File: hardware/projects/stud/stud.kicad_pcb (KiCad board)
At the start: 2 copper layers, 3 parts, among them IC1 R7KA8M2JFLCAC#UC0, U1 IS42VM32160E-75BLI, U2 TAC5242

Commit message: switch to four layers
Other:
- copper layers 2 -> 4
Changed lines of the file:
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@@
 	(layers
 		(0 "F.Cu" signal)
+		(4 "In1.Cu" signal)
+		(6 "In2.Cu" signal)
 		(2 "B.Cu" signal)
 		(9 "F.Adhes" user "F.Adhesive")
@@
 			)
 			(layer "dielectric 1"
-				(type "core")
-				(thickness 1.51)
+				(type "prepreg")
+				(thickness 0.1)
 				(material "FR4")
 				(epsilon_r 4.5)
+				(loss_tangent 0.02)
+			)
+			(layer "In1.Cu"
+				(type "copper")
+				(thickness 0.035)
+			)
+			(layer "dielectric 2"
+				(type "core")
+				(thickness 1.24)
+				(material "FR4")
+				(epsilon_r 4.5)
+				(loss_tangent 0.02)
+			)
+			(layer "In2.Cu"
+				(type "copper")
+				(thickness 0.035)
+			)
+			(layer "dielectric 3"
+				(type "prepreg")
+				(thickness 0.1)
+				(material "FR4")
+				(epsilon_r 4.5)

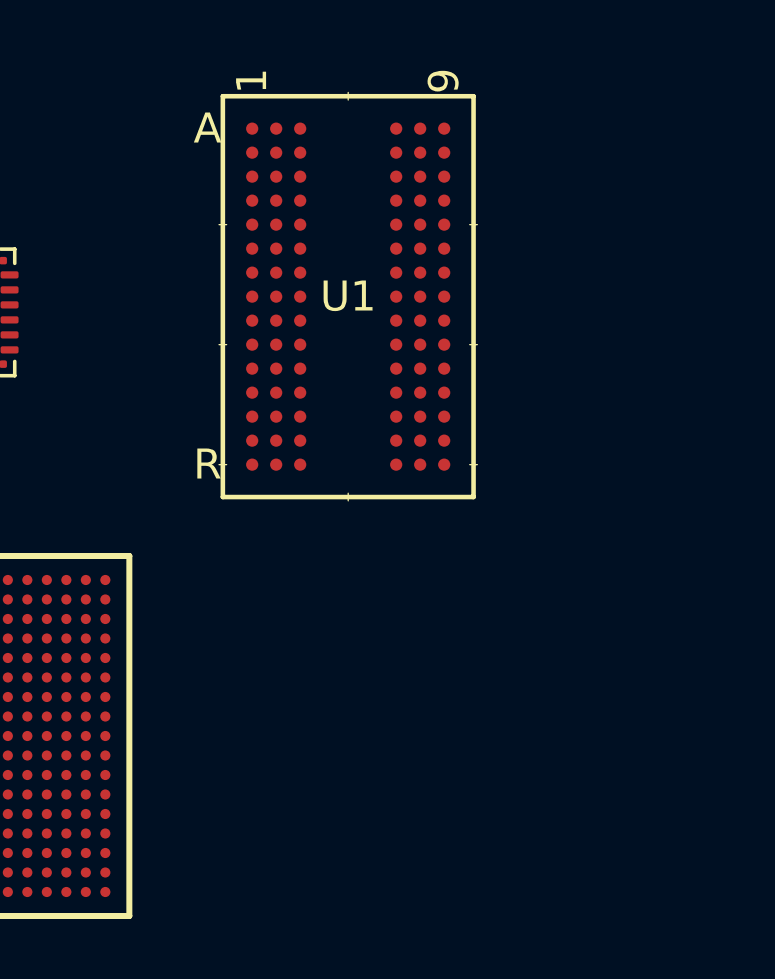
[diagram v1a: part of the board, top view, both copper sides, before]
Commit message: switch SDRAM chips at fable's behest
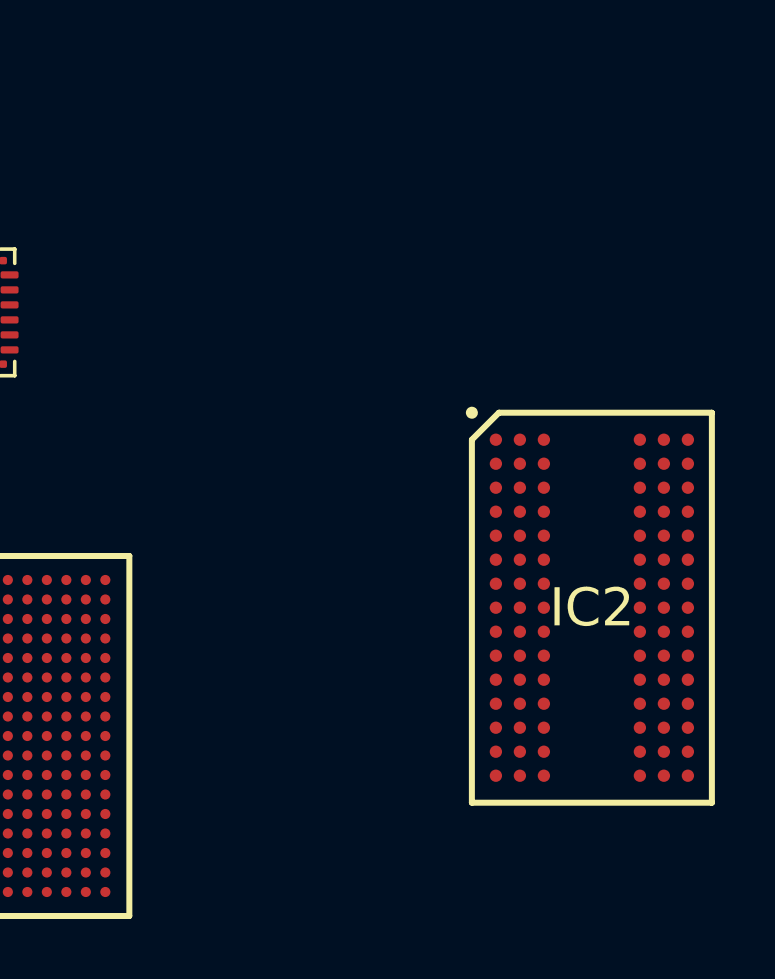
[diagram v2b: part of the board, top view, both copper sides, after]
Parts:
- removed U1: IS42VM32160E-75BLI, vendor:TFBGA-90_8X13_ISI
- added IC2: IS42S32160F-7BLI, vendor:BGA90C80P9X15_800X1300X120, F.Cu at (155.4, 106.9)

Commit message: think about routing SDRAM traces
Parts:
- moved IC2 8.45 mm to (147.3, 109.2)
- moved IC1 2.03 mm to (134.6, 109.2)
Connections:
- IC1 pad L3: unconnected-(IC1-PC04-PadL3) -> DQ26
- IC1 pad L4: unconnected-(IC1-PC09-PadL4) -> DQ21
- IC1 pad L5: unconnected-(IC1-PC05-PadL5) -> DQ25
- IC2 pad A1: unconnected-(IC2-DQ26-PadA1) -> DQ26
- IC2 pad A9: unconnected-(IC2-DQ21-PadA9) -> DQ21
- IC2 pad C3: unconnected-(IC2-DQ25-PadC3) -> DQ25
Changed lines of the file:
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@@
 	(layers
 		(0 "F.Cu" signal)
-		(4 "In1.Cu" signal)
-		(6 "In2.Cu" signal)
+		(4 "In1.Cu" power)
+		(6 "In2.Cu" power)
 		(2 "B.Cu" signal)
 		(9 "F.Adhes" user "F.Adhesive")
@@
 	(footprint "vendor:BGA90C80P9X15_800X1300X120"
 		(layer "F.Cu")
-		(at 155.443 106.889)
+		(at 147.32 109.22)
 		(descr "90L 8x13mm TF-BGA")
 		(tags "Integrated Circuit")
@@
 		(sheetname "/")
 		(sheetfile "stud.kicad_sch")
+		(units
+			(unit
+				(name "A")
+				(pins "A1" "A2" "A3" "A7" "A8" "A9" "B1" "B2" "B3" "B7" "B8" "B9" "C1"
+					"C2" "C3" "C7" "C8" "C9" "D1" "D2" "D3" "D7" "D8" "D9" "E1" "E2" "E3"
+					"E7" "E8" "E9" "F1" "F2" "F3" "F7" "F8" "F9" "G1" "G2" "G3" "G7" "G8"
+					"G9" "H1" "H2" "H3" "H7" "H8" "H9" "J1" "J2" "J3" "J7" "J8" "J9" "K1"
+					"K2" "K3" "K7" "K8" "K9" "L1" "L2" "L3" "L7" "L8" "L9" "M1" "M2" "M3"
+					"M7" "M8" "M9" "N1" "N2" "N3" "N7" "N8" "N9" "P1" "P2" "P3" "P7" "P8"
+					"P9" "R1" "R2" "R3" "R7" "R8" "R9"
+				)
+			)
+		)
 		(solder_mask_margin 0.035)
 		(attr smd)
@@
 			(size 0.41 0.41)
 			(layers "F.Cu" "F.Mask" "F.Paste")
-			(net "unconnected-(IC2-DQ26-PadA1)")
+			(net "DQ26")
 			(pinfunction "DQ26_A1")
 			(pintype "passive")
@@
 			(size 0.41 0.41)
 			(layers "F.Cu" "F.Mask" "F.Paste")
-			(net "unconnected-(IC2-DQ21-PadA9)")
+			(net "DQ21")
 			(pinfunction "DQ21_A9")
 			(pintype "passive")
@@
 			(size 0.41 0.41)
 			(layers "F.Cu" "F.Mask" "F.Paste")
-			(net "unconnected-(IC2-DQ25-PadC3)")
+			(net "DQ25")
 			(pinfunction "DQ25_C3")
 			(pintype "passive")
@@
 	(footprint "vendor:BGA289C65P17X17_1200X1200X138"
 		(layer "F.Cu")
-		(at 134.025 111.165)
+		(at 134.62 109.22)
 		(descr "PLBG0289JA-A")
 		(tags "Integrated Circuit")
@@
 			(size 0.338 0.338)
 			(layers "F.Cu" "F.Mask" "F.Paste")
-			(net "unconnected-(IC1-PC04-PadL3)")
+			(net "DQ26")
 			(pinfunction "PC04_L3")
 			(pintype "passive")
@@
 			(size 0.338 0.338)
 			(layers "F.Cu" "F.Mask" "F.Paste")
-			(net "unconnected-(IC1-PC09-PadL4)")
+			(net "DQ21")
 			(pinfunction "PC09_L4")
 			(pintype "passive")
@@
 			(size 0.338 0.338)
 			(layers "F.Cu" "F.Mask" "F.Paste")
-			(net "unconnected-(IC1-PC05-PadL5)")
+			(net "DQ25")
 			(pinfunction "PC05_L5")
 			(pintype "passive")

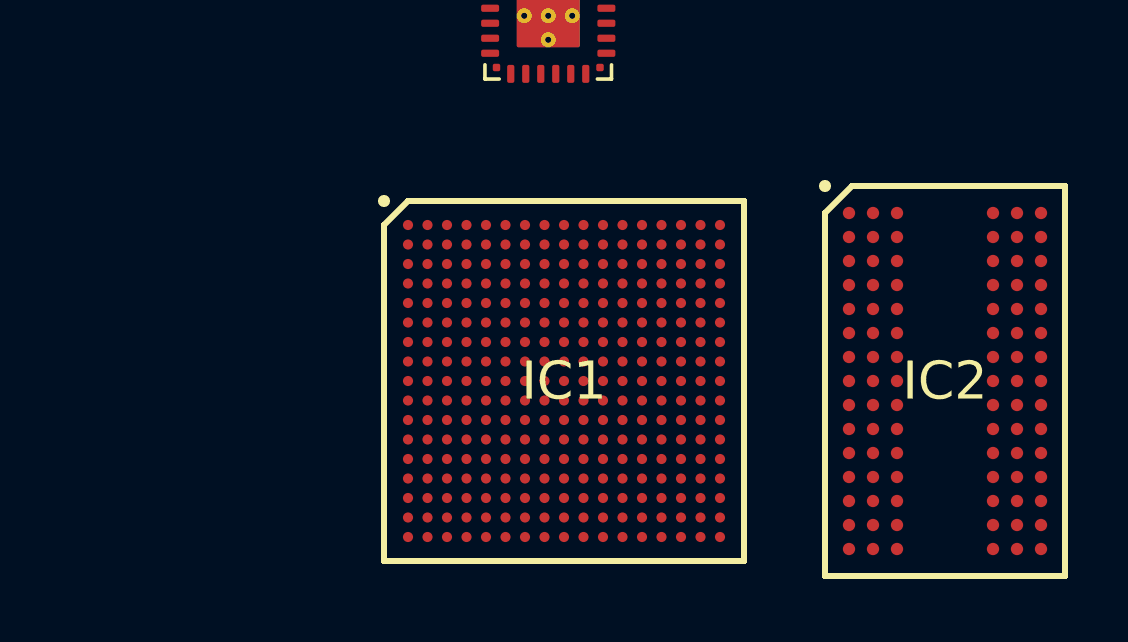
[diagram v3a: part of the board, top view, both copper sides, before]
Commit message: add enough DQ nets to peek at connections
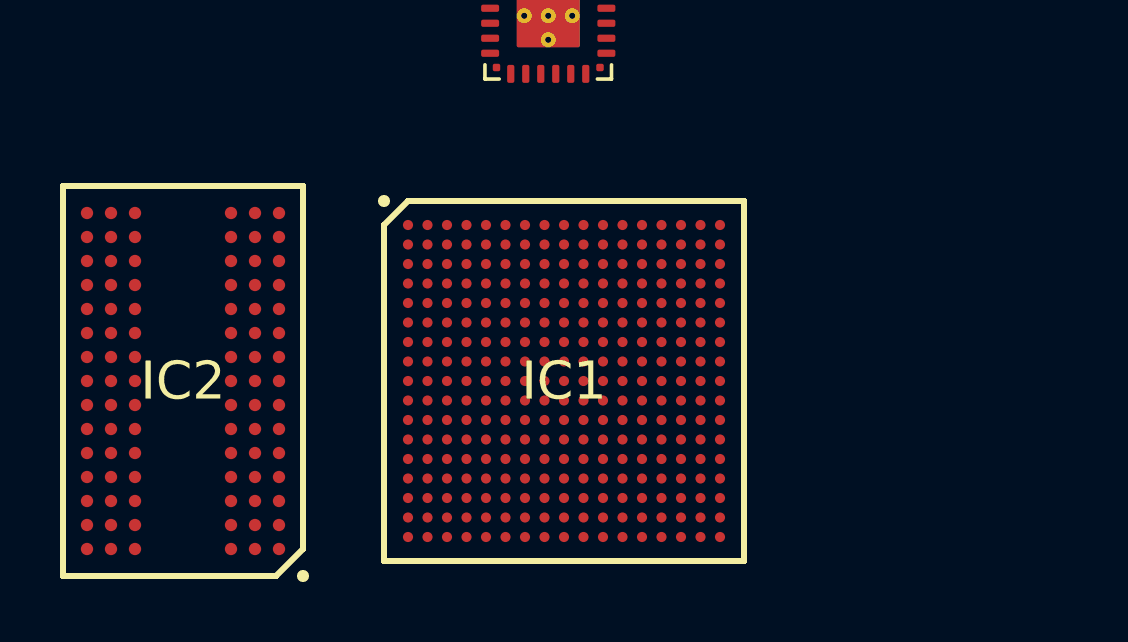
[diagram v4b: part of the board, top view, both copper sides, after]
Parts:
- moved IC2 25.4 mm to (121.9, 109.2), turned to 180 degrees
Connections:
- IC1 pad A1: unconnected-(IC1-P609-PadA1) -> DQ7
- IC1 pad A2: unconnected-(IC1-P113-PadA2) -> DQ4
- IC1 pad A3: unconnected-(IC1-P115-PadA3) -> DQ6
- IC1 pad A4: unconnected-(IC1-P112-PadA4) -> DQ3
- IC1 pad A5: unconnected-(IC1-P302-PadA5) -> DQ0
- IC1 pad B2: unconnected-(IC1-PA12-PadB2) -> DQ9
- IC1 pad B3: unconnected-(IC1-P114-PadB3) -> DQ5
- IC1 pad B4: unconnected-(IC1-PA11-PadB4) -> DQ8
- IC1 pad B5: unconnected-(IC1-P300-PadB5) -> DQ2
- IC1 pad C3: unconnected-(IC1-PA13-PadC3) -> DQ15
- IC2 pad A2: unconnected-(IC2-DQ24-PadA2) -> DQ24
- IC2 pad A8: unconnected-(IC2-DQ23-PadA8) -> DQ23
- IC2 pad B1: unconnected-(IC2-DQ28-PadB1) -> DQ28
- IC2 pad B9: unconnected-(IC2-DQ19-PadB9) -> DQ19
- IC2 pad C2: unconnected-(IC2-DQ27-PadC2) -> DQ27
- IC2 pad C7: unconnected-(IC2-DQ22-PadC7) -> DQ22
- IC2 pad C8: unconnected-(IC2-DQ20-PadC8) -> DQ20
- IC2 pad D2: unconnected-(IC2-DQ29-PadD2) -> DQ29
- IC2 pad D3: unconnected-(IC2-DQ30-PadD3) -> DQ30
- IC2 pad D7: unconnected-(IC2-DQ17-PadD7) -> DQ17
- IC2 pad D8: unconnected-(IC2-DQ18-PadD8) -> DQ18
- IC2 pad E2: unconnected-(IC2-DQ31-PadE2) -> DQ31
- IC2 pad E8: unconnected-(IC2-DQ16-PadE8) -> DQ16
- IC2 pad L2: unconnected-(IC2-DQ8-PadL2) -> DQ8
- IC2 pad L8: unconnected-(IC2-DQ7-PadL8) -> DQ7
- IC2 pad M2: unconnected-(IC2-DQ10-PadM2) -> DQ10
- IC2 pad M3: unconnected-(IC2-DQ9-PadM3) -> DQ9
- IC2 pad M7: unconnected-(IC2-DQ6-PadM7) -> DQ6
- IC2 pad M8: unconnected-(IC2-DQ5-PadM8) -> DQ5
- IC2 pad N2: unconnected-(IC2-DQ12-PadN2) -> DQ12
- IC2 pad N3: unconnected-(IC2-DQ14-PadN3) -> DQ14
- IC2 pad N7: unconnected-(IC2-DQ1-PadN7) -> DQ1
- IC2 pad N8: unconnected-(IC2-DQ3-PadN8) -> DQ3
- IC2 pad P1: unconnected-(IC2-DQ11-PadP1) -> DQ11
- IC2 pad P9: unconnected-(IC2-DQ4-PadP9) -> DQ4
- IC2 pad R1: unconnected-(IC2-DQ13-PadR1) -> DQ13
- IC2 pad R2: unconnected-(IC2-DQ15-PadR2) -> DQ15
- IC2 pad R8: unconnected-(IC2-DQ0-PadR8) -> DQ0
- IC2 pad R9: unconnected-(IC2-DQ2-PadR9) -> DQ2

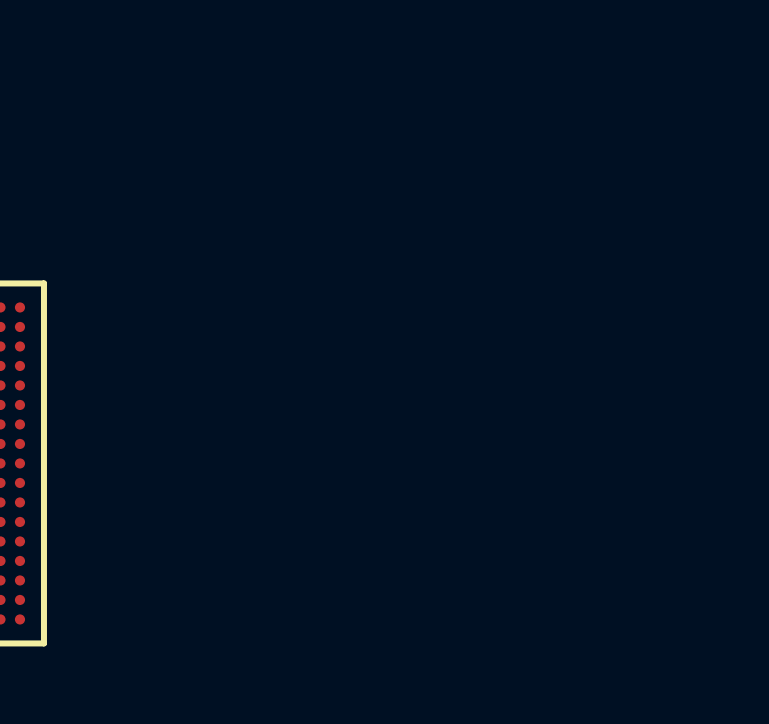
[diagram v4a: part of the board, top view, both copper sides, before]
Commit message: add a microSD connector
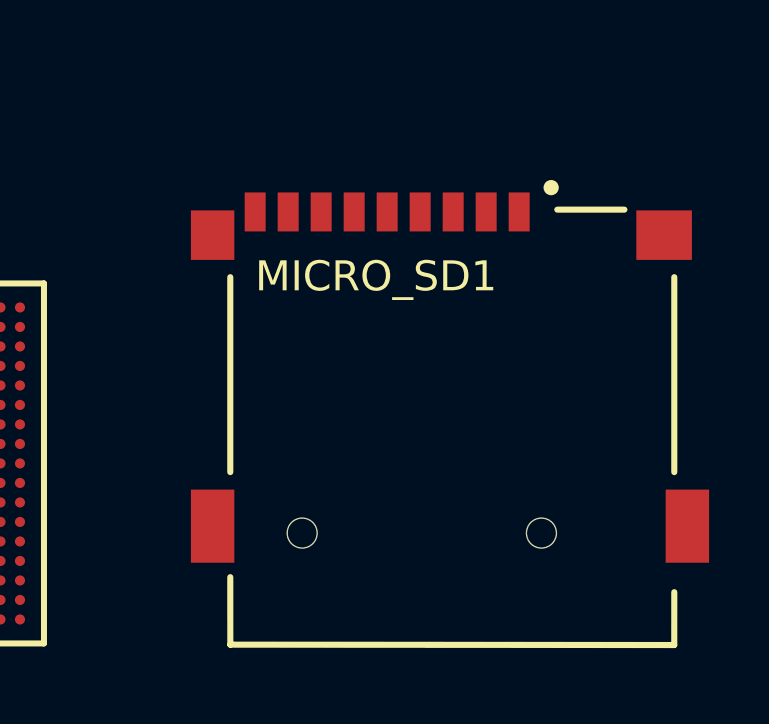
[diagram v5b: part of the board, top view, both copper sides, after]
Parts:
- added MICRO_SD1: TF-01A, vendor:TF-01A, F.Cu at (154.2, 108.0)

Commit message: add a buck converter
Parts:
- added U1: TPS629210DRLR, vendor:SOT50P160X60-8N, F.Cu at (141.5, 95.3)

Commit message: add a castellated edge gpio footprint
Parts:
- added J1: USB_C_Receptacle_USB2.0_16P, Connector_USB:USB_C_Receptacle_G-Switch_GT-USB-7010ASV, F.Cu at (180.6, 106.5)
- added Y1: X1G0044510004, custom:SG5032CAN, F.Cu at (178.3, 113.7)
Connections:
- IC1 pad A10: unconnected-(IC1-VCC_D_CDC_1-PadA10) -> +3V3
- IC1 pad A11: unconnected-(IC1-VCC_D_CDC_2-PadA11) -> +3V3
- IC1 pad A7: unconnected-(IC1-VLO_1-PadA7) -> VLO
- IC1 pad A8: unconnected-(IC1-VLO_2-PadA8) -> VLO
- IC1 pad A9: unconnected-(IC1-VSS_D_CDC_1-PadA9) -> GND
- IC1 pad B1: unconnected-(IC1-P813-PadB1) -> SDCS
- IC1 pad B10: unconnected-(IC1-VCC_D_CDC_3-PadB10) -> +3V3
- IC1 pad B11: unconnected-(IC1-VCC_D_CDC_4-PadB11) -> +3V3
- IC1 pad B16: unconnected-(IC1-PD01-PadB16) -> μSD_DAT2
- IC1 pad B17: unconnected-(IC1-PD02-PadB17) -> μSD_DAT1
- IC1 pad B7: unconnected-(IC1-VLO_3-PadB7) -> VLO
- IC1 pad B8: unconnected-(IC1-VLO_4-PadB8) -> VLO
- IC1 pad B9: unconnected-(IC1-VSS_D_CDC_2-PadB9) -> GND
- IC1 pad C1: unconnected-(IC1-PA06-PadC1) -> CKE
- IC1 pad C14: unconnected-(IC1-PD04-PadC14) -> μSD_CMD
- IC1 pad C15: unconnected-(IC1-PD03-PadC15) -> μSD_DAT0
- IC1 pad C16: unconnected-(IC1-PD05-PadC16) -> μSD_CLK
- IC1 pad C2: unconnected-(IC1-P613-PadC2) -> DQ15
- IC1 pad C3: DQ15 -> DQ10
- IC1 pad C4: unconnected-(IC1-P301-PadC4) -> DQ1
- IC1 pad D1: unconnected-(IC1-PA04-PadD1) -> DQM3
- IC1 pad D11: unconnected-(IC1-P306-PadD11) -> μSD_CD
- IC1 pad D2: unconnected-(IC1-P611-PadD2) -> DQ13
- IC1 pad D3: unconnected-(IC1-P610-PadD3) -> DQ12
- IC1 pad D4: unconnected-(IC1-PA14-PadD4) -> DQ11
- IC1 pad E1: unconnected-(IC1-PA15-PadE1) -> SDCLK
- IC1 pad E2: unconnected-(IC1-P615-PadE2) -> DQM2
- IC1 pad E3: unconnected-(IC1-P614-PadE3) -> DQM0
- IC1 pad E4: unconnected-(IC1-P612-PadE4) -> DQ14
- IC1 pad E8: unconnected-(IC1-P111-PadE8) -> μSD_DAT3
- IC1 pad F1: unconnected-(IC1-PA02-PadF1) -> A3
- IC1 pad F10: unconnected-(IC1-VSS_07-PadF10) -> GND
- IC1 pad F11: unconnected-(IC1-VCC_07-PadF11) -> +3V3
- IC1 pad F14: unconnected-(IC1-P406-PadF14) -> SSI_RX
- IC1 pad F2: unconnected-(IC1-PA10-PadF2) -> RAS
- IC1 pad F3: unconnected-(IC1-PA08-PadF3) -> WE
- IC1 pad F4: unconnected-(IC1-PA09-PadF4) -> CAS
- IC1 pad F5: unconnected-(IC1-PC14-PadF5) -> DQ16
- IC1 pad F6: unconnected-(IC1-VCC_08-PadF6) -> +3V3
- IC1 pad F7: unconnected-(IC1-VSS_08-PadF7) -> GND
- IC1 pad F8: unconnected-(IC1-VSS3-PadF8) -> GND
- IC1 pad G1: unconnected-(IC1-PA00-PadG1) -> A5
- IC1 pad G10: unconnected-(IC1-VSS_06-PadG10) -> GND
- IC1 pad G11: unconnected-(IC1-VCC_06-PadG11) -> +3V3
- IC1 pad G12: unconnected-(IC1-P405-PadG12) -> SSI_TX
- IC1 pad G15: unconnected-(IC1-VSS_03-PadG15) -> GND
- IC1 pad G16: unconnected-(IC1-VCC_05-PadG16) -> +3V3
- IC1 pad G17: unconnected-(IC1-VSS_05-PadG17) -> GND
- IC1 pad G2: unconnected-(IC1-PA03-PadG2) -> A2
- IC1 pad G3: unconnected-(IC1-PA05-PadG3) -> DQM1
- IC1 pad G5: unconnected-(IC1-PC12-PadG5) -> DQ18
- IC1 pad G6: unconnected-(IC1-VCC_09-PadG6) -> +3V3
- IC1 pad G7: unconnected-(IC1-VSS_09-PadG7) -> GND
- IC1 pad G8: unconnected-(IC1-VSS4-PadG8) -> GND
- IC1 pad G9: unconnected-(IC1-VCL4-PadG9) -> +0V9
- IC1 pad H1: unconnected-(IC1-P504-PadH1) -> A7
- IC1 pad H10: unconnected-(IC1-VSS5-PadH10) -> GND
- IC1 pad H11: unconnected-(IC1-VCC_04-PadH11) -> +3V3
- IC1 pad H12: unconnected-(IC1-VSS_04-PadH12) -> GND
- IC1 pad H13: unconnected-(IC1-P403-PadH13) -> SSI_BCK
- IC1 pad H14: unconnected-(IC1-VCC_03-PadH14) -> +3V3
- IC1 pad H15: unconnected-(IC1-VCC_USBHS-PadH15) -> +3V3
- IC1 pad H16: unconnected-(IC1-USBH_S_DP-PadH16) -> USB_D+
- IC1 pad H17: unconnected-(IC1-USBH_S_DM-PadH17) -> USB_D-
- IC1 pad H2: unconnected-(IC1-P503-PadH2) -> A6
- IC1 pad H3: unconnected-(IC1-P505-PadH3) -> A8
- IC1 pad H4: unconnected-(IC1-PA01-PadH4) -> A4
- IC1 pad H5: unconnected-(IC1-PC11-PadH5) -> DQ19
- IC1 pad H6: unconnected-(IC1-VCC_10-PadH6) -> +3V3
- IC1 pad H7: unconnected-(IC1-VSS_10-PadH7) -> GND
- IC1 pad H8: unconnected-(IC1-VSS7-PadH8) -> GND
- IC1 pad H9: unconnected-(IC1-VCL5-PadH9) -> +0V9
- IC1 pad J1: unconnected-(IC1-P506-PadJ1) -> A9
- IC1 pad J10: unconnected-(IC1-VSS6-PadJ10) -> GND
- IC1 pad J12: unconnected-(IC1-VSS2-PadJ12) -> GND
- IC1 pad J13: unconnected-(IC1-P404-PadJ13) -> SSI_FS
- IC1 pad J14: unconnected-(IC1-VSS_0_2-PadJ14) -> GND
- IC1 pad J15: unconnected-(IC1-USBH_S_RRE_F-PadJ15) -> Net-(IC1-USBHS_RREF)
- IC1 pad J16: unconnected-(IC1-VSS2__USBH_S-PadJ16) -> GND
- IC1 pad J17: unconnected-(IC1-VSS1__USBH_S-PadJ17) -> GND
- IC1 pad J2: unconnected-(IC1-P507-PadJ2) -> A10
- IC1 pad J3: unconnected-(IC1-P508-PadJ3) -> A11
- IC1 pad J4: unconnected-(IC1-P509-PadJ4) -> A12
- IC1 pad J5: unconnected-(IC1-PC13-PadJ5) -> DQ17
- IC1 pad J6: unconnected-(IC1-VCC2__11-PadJ6) -> +3V3
- IC1 pad J7: unconnected-(IC1-VSS_1_1-PadJ7) -> GND
- IC1 pad J8: unconnected-(IC1-VCL7-PadJ8) -> +0V9
- IC1 pad J9: unconnected-(IC1-VCL6-PadJ9) -> +0V9
- IC1 pad K1: unconnected-(IC1-PC15-PadK1) -> A16
- IC1 pad K10: unconnected-(IC1-VSS8-PadK10) -> GND
- IC1 pad K11: unconnected-(IC1-VCL1-PadK11) -> +0V9
- IC1 pad K12: unconnected-(IC1-VSS1-PadK12) -> GND
- IC1 pad K14: unconnected-(IC1-VCC_0_2-PadK14) -> +3V3
- IC1 pad K15: unconnected-(IC1-AVCC__USBH_S-PadK15) -> +3V3
- IC1 pad K17: unconnected-(IC1-P212/E_XTAL-PadK17) -> EXTAL
- IC1 pad K2: unconnected-(IC1-P608-PadK2) -> A14
- IC1 pad K3: unconnected-(IC1-P510-PadK3) -> A13
- IC1 pad K4: unconnected-(IC1-PD00-PadK4) -> A15
- IC1 pad K5: unconnected-(IC1-PC07-PadK5) -> DQ23
- IC1 pad K6: unconnected-(IC1-VSS_1_2-PadK6) -> GND
- IC1 pad K7: unconnected-(IC1-VSS9-PadK7) -> GND
- IC1 pad K8: unconnected-(IC1-VCL9-PadK8) -> +0V9
- IC1 pad K9: unconnected-(IC1-VCL8-PadK9) -> +0V9
- IC1 pad L1: unconnected-(IC1-PC03-PadL1) -> DQ27
- IC1 pad L11: unconnected-(IC1-VCL0-PadL11) -> +0V9
- IC1 pad L12: unconnected-(IC1-VSS0-PadL12) -> GND
- IC1 pad L15: unconnected-(IC1-VCC_0_1-PadL15) -> +3V3
- IC1 pad L2: unconnected-(IC1-PC02-PadL2) -> DQ28
- IC1 pad L6: unconnected-(IC1-VCC2__12-PadL6) -> +3V3
- IC1 pad L7: unconnected-(IC1-VSS_1_4-PadL7) -> GND
- IC1 pad L8: unconnected-(IC1-VSS_1_5-PadL8) -> GND
- IC1 pad L9: unconnected-(IC1-VSS10-PadL9) -> GND
- IC1 pad M1: unconnected-(IC1-PC00-PadM1) -> DQ30
- IC1 pad M10: unconnected-(IC1-VSS11-PadM10) -> GND
- IC1 pad M11: unconnected-(IC1-VCL11-PadM11) -> +0V9
- IC1 pad M15: unconnected-(IC1-P408-PadM15) -> VBUS
- IC1 pad M17: unconnected-(IC1-VSS_0_1-PadM17) -> GND
- IC1 pad M2: unconnected-(IC1-P607-PadM2) -> DQ31
- IC1 pad M3: unconnected-(IC1-PC01-PadM3) -> DQ29
- IC1 pad M4: unconnected-(IC1-PC08-PadM4) -> DQ22
- IC1 pad M5: unconnected-(IC1-PC10-PadM5) -> DQ20
- IC1 pad M7: unconnected-(IC1-VCC2__14-PadM7) -> +3V3
- IC1 pad M8: unconnected-(IC1-VCC2__15-PadM8) -> +3V3
- IC1 pad N4: unconnected-(IC1-PC06-PadN4) -> DQ24
- IC1 pad R1: unconnected-(IC1-VCC2__13-PadR1) -> +3V3
- IC1 pad T17: unconnected-(IC1-VSS_U_SB-PadT17) -> GND
- IC1 pad U17: unconnected-(IC1-VCC_U_SB-PadU17) -> +3V3
- IC1 pad U4: unconnected-(IC1-VSS_1_3-PadU4) -> GND
- IC2 pad A3: unconnected-(IC2-VSS_1-PadA3) -> GND
- IC2 pad A7: unconnected-(IC2-VDD_1-PadA7) -> +3V3
- IC2 pad B2: unconnected-(IC2-VDDQ_1-PadB2) -> +3V3
- IC2 pad B3: unconnected-(IC2-VSSQ_1-PadB3) -> GND
- IC2 pad B7: unconnected-(IC2-VDDQ_2-PadB7) -> +3V3
- IC2 pad B8: unconnected-(IC2-VSSQ_2-PadB8) -> GND
- IC2 pad C1: unconnected-(IC2-VSSQ_3-PadC1) -> GND
- IC2 pad C9: unconnected-(IC2-VDDQ_3-PadC9) -> +3V3
- IC2 pad D1: unconnected-(IC2-VSSQ_4-PadD1) -> GND
- IC2 pad D9: unconnected-(IC2-VDDQ_4-PadD9) -> +3V3
- IC2 pad E1: unconnected-(IC2-VDDQ_5-PadE1) -> +3V3
- IC2 pad E9: unconnected-(IC2-VSSQ_5-PadE9) -> GND
- IC2 pad F1: unconnected-(IC2-VSS_2-PadF1) -> GND
- IC2 pad F2: unconnected-(IC2-DQM3-PadF2) -> DQM3
- IC2 pad F3: unconnected-(IC2-A3-PadF3) -> A5
- IC2 pad F7: unconnected-(IC2-A2-PadF7) -> A4
- IC2 pad F8: unconnected-(IC2-DQM2-PadF8) -> DQM2
- IC2 pad F9: unconnected-(IC2-VDD_2-PadF9) -> +3V3
- IC2 pad G1: unconnected-(IC2-A4-PadG1) -> A6
- IC2 pad G2: unconnected-(IC2-A5-PadG2) -> A7
- IC2 pad G3: unconnected-(IC2-A6-PadG3) -> A8
- IC2 pad G7: unconnected-(IC2-A10-PadG7) -> A12
- IC2 pad G8: unconnected-(IC2-A0-PadG8) -> A2
- IC2 pad G9: unconnected-(IC2-A1-PadG9) -> A3
- IC2 pad H1: unconnected-(IC2-A7-PadH1) -> A9
- IC2 pad H2: unconnected-(IC2-A8-PadH2) -> A10
- IC2 pad H3: unconnected-(IC2-A12-PadH3) -> A14
- IC2 pad H8: unconnected-(IC2-BA1-PadH8) -> A16
- IC2 pad H9: unconnected-(IC2-A11-PadH9) -> A13
- IC2 pad J1: unconnected-(IC2-CLK-PadJ1) -> SDCLK
- IC2 pad J2: unconnected-(IC2-CKE-PadJ2) -> CKE
- IC2 pad J3: unconnected-(IC2-A9-PadJ3) -> A11
- IC2 pad J7: unconnected-(IC2-BA0-PadJ7) -> A15
- IC2 pad J8: unconnected-(IC2-~{CS}-PadJ8) -> SDCS
- IC2 pad J9: unconnected-(IC2-~{RAS}-PadJ9) -> RAS
- IC2 pad K1: unconnected-(IC2-DQM1-PadK1) -> DQM1
- IC2 pad K7: unconnected-(IC2-~{CAS}-PadK7) -> CAS
- IC2 pad K8: unconnected-(IC2-~{WE}-PadK8) -> WE
- IC2 pad K9: unconnected-(IC2-DQM0-PadK9) -> DQM0
- IC2 pad L1: unconnected-(IC2-VDDQ_6-PadL1) -> +3V3
- IC2 pad L3: unconnected-(IC2-VSS_3-PadL3) -> GND
- IC2 pad L7: unconnected-(IC2-VDD_3-PadL7) -> +3V3
- IC2 pad L9: unconnected-(IC2-VSSQ_6-PadL9) -> GND
- IC2 pad M1: unconnected-(IC2-VSSQ_7-PadM1) -> GND
- IC2 pad M9: unconnected-(IC2-VDDQ_7-PadM9) -> +3V3
- IC2 pad N1: unconnected-(IC2-VSSQ_8-PadN1) -> GND
- IC2 pad N9: unconnected-(IC2-VDDQ_8-PadN9) -> +3V3
- IC2 pad P2: unconnected-(IC2-VDDQ_9-PadP2) -> +3V3
- IC2 pad P3: unconnected-(IC2-VSSQ_9-PadP3) -> GND
- IC2 pad P7: unconnected-(IC2-VDDQ_10-PadP7) -> +3V3
- IC2 pad P8: unconnected-(IC2-VSSQ_10-PadP8) -> GND
- IC2 pad R3: unconnected-(IC2-VSS_4-PadR3) -> GND
- IC2 pad R7: unconnected-(IC2-VDD_4-PadR7) -> +3V3
- MICRO_SD1 pad 1: unconnected-(MICRO_SD1-DAT2-Pad1) -> μSD_DAT2
- MICRO_SD1 pad 2: unconnected-(MICRO_SD1-CD/DAT3-Pad2) -> μSD_DAT3
- MICRO_SD1 pad 3: unconnected-(MICRO_SD1-CMD-Pad3) -> μSD_CMD
- MICRO_SD1 pad 4: unconnected-(MICRO_SD1-VDD-Pad4) -> +3V3
- MICRO_SD1 pad 5: unconnected-(MICRO_SD1-CLK-Pad5) -> μSD_CLK
- MICRO_SD1 pad 6: unconnected-(MICRO_SD1-VSS-Pad6) -> GND
- MICRO_SD1 pad 7: unconnected-(MICRO_SD1-DAT0-Pad7) -> μSD_DAT0
- MICRO_SD1 pad 8: unconnected-(MICRO_SD1-DAT1-Pad8) -> μSD_DAT1
- MICRO_SD1 pad CD1: unconnected-(MICRO_SD1-CD-PadCD1) -> μSD_CD
- MICRO_SD1 pad MP1: SHIELD -> GND
- MICRO_SD1 pad MP2: SHIELD -> GND
- MICRO_SD1 pad MP3: SHIELD -> GND
- MICRO_SD1 pad MP4: SHIELD -> GND
- U1 pad 3: unconnected-(U1-VOS-Pad3) -> +3V3
- U1 pad 4: unconnected-(U1-SW-Pad4) -> Net-(U1-SW)
- U1 pad 5: unconnected-(U1-GND-Pad5) -> GND
- U1 pad 6: unconnected-(U1-VIN-Pad6) -> VDC
- U1 pad 7: unconnected-(U1-EN-Pad7) -> VDC
- U1 pad 8: unconnected-(U1-MODE/S-CONF-Pad8) -> GND
- U2 pad 1: unconnected-(U2-DREG-Pad1) -> Net-(U2-DREG)
- U2 pad 10: unconnected-(U2-MD4-Pad10) -> GND
- U2 pad 11: unconnected-(U2-GPO-Pad11) -> CODEC_ERROR
- U2 pad 12: unconnected-(U2-MD5-Pad12) -> +3V3
- U2 pad 13: unconnected-(U2-MD0-Pad13) -> GND
- U2 pad 14: unconnected-(U2-MICBIAS-Pad14) -> Net-(U2-MICBIAS)
- U2 pad 15: unconnected-(U2-IN1P-Pad15) -> Net-(U2-IN1P)
- U2 pad 16: unconnected-(U2-IN1M-Pad16) -> Net-(U2-IN1M)
- U2 pad 17: unconnected-(U2-IN2P-Pad17) -> Net-(U2-IN2P)
- U2 pad 18: unconnected-(U2-IN2M-Pad18) -> Net-(U2-IN2M)
- U2 pad 2: unconnected-(U2-BCLK-Pad2) -> SSI_BCK
- U2 pad 20: unconnected-(U2-OUT1P-Pad20) -> Net-(U2-OUT1P)
- U2 pad 21: unconnected-(U2-OUT2P-Pad21) -> Net-(U2-OUT2P)
- U2 pad 23: unconnected-(U2-AVDD-Pad23) -> +3V3A
- U2 pad 24: unconnected-(U2-VREF-Pad24) -> Net-(U2-VREF)
- U2 pad 3: unconnected-(U2-FSYNC-Pad3) -> SSI_FS
- U2 pad 4: unconnected-(U2-DOUT-Pad4) -> SSI_RX
- U2 pad 5: unconnected-(U2-DIN-Pad5) -> SSI_TX
- U2 pad 6: unconnected-(U2-IOVDD-Pad6) -> +3V3
- U2 pad 7: unconnected-(U2-MD1-Pad7) -> GND
- U2 pad 8: unconnected-(U2-MD2-Pad8) -> GND
- U2 pad 9: unconnected-(U2-MD3-Pad9) -> GND
- U2 pad A1: unconnected-(U2-VSS-PadA1) -> GNDA
- U2 pad A2: unconnected-(U2-VSS-PadA2) -> GNDA
- U2 pad A3: unconnected-(U2-VSS-PadA3) -> GNDA
- U2 pad A4: unconnected-(U2-VSS-PadA4) -> GNDA
- U2 pad TP: unconnected-(U2-VSS-PadTP) -> GNDA
